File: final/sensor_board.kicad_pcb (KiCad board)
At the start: 2 copper layers, 75 parts, among them J1 USB_microB_2040002-1, J2 Arduino_ICSP, J3 Conn_01x02_Male, J6 BT CONFIG, SW1 SW_DIP_x01, U1 NC7SZ04P5X, U10 BQ24075, U11 BQ27441-G1, U2 MCP1702T-3302E/CBCT-ND, U3 TXS0104E, U4 TPS61200DRC, U5 FT232RL, U6 RN4871, U7 TPS2113ADRBR, U8 US5881, U9 ATMEGA328PB-ANR, Y1 16MHz

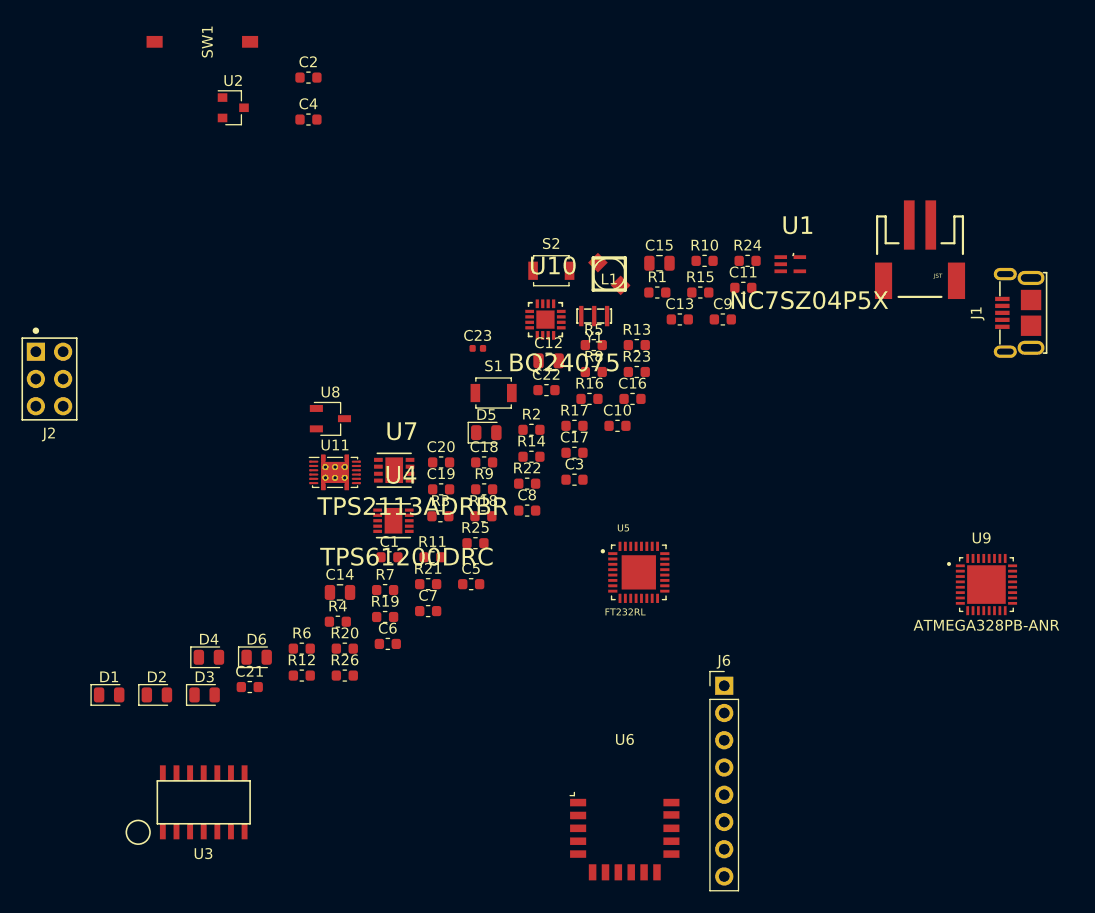
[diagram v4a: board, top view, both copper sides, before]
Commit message: sensor board layout complete
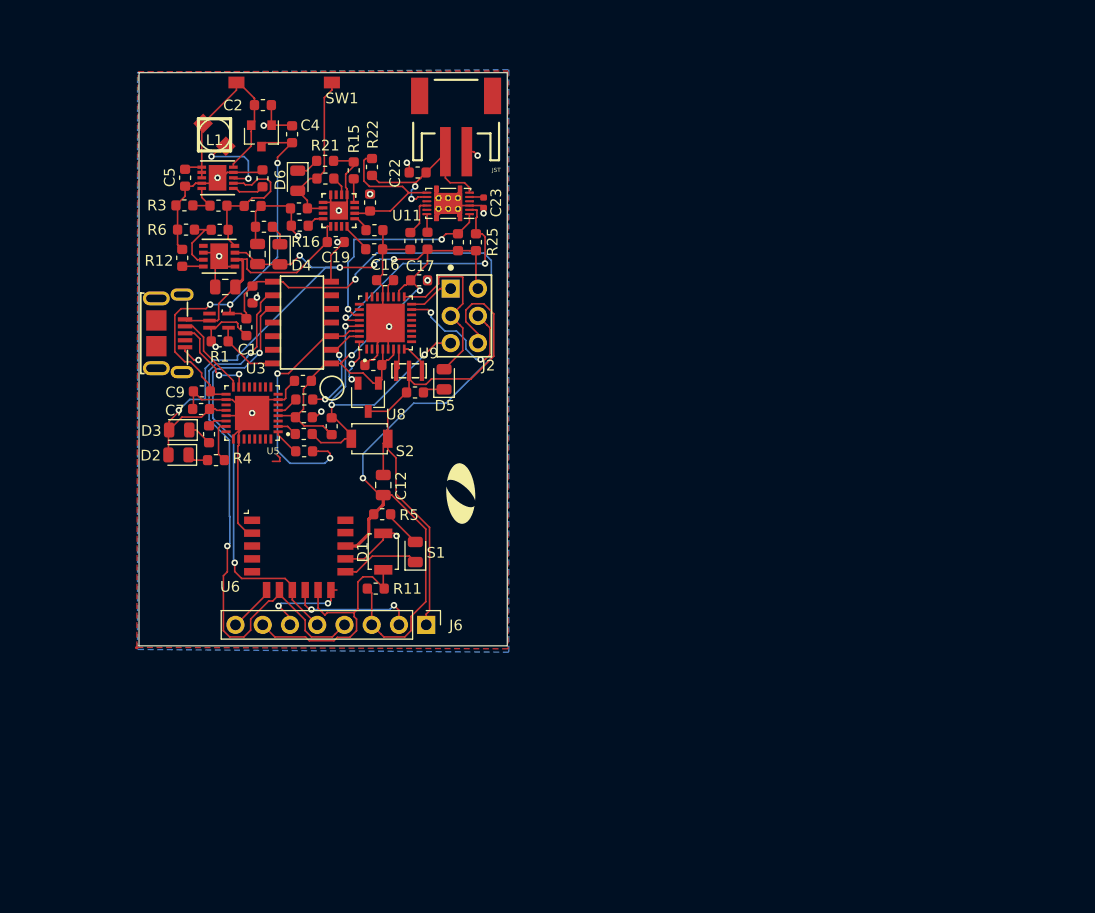
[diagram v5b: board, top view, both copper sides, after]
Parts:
- added OlinLogo: G***, mp3b:OlinLogo, F.Cu at (148.6, 100.7)
- moved J1 81.6 mm to (120.2, 85.8), turned to 270 degrees
- moved U9 61.1 mm to (141.6, 84.8), turned to 90 degrees
- moved U1 53.5 mm to (126.1, 84.6)
- moved C9 49.0 mm to (124.5, 91.2), turned to 180 degrees
- moved C21 46.5 mm to (140.2, 73.6), turned to 270 degrees
- moved C11 46.4 mm to (129.2, 73.9)
- moved C5 46.3 mm to (122.9, 71.2), turned to 270 degrees
- moved U3 45.7 mm to (133.8, 84.7), turned to 90 degrees
- moved J3 45.5 mm to (148.2, 65.1), turned to 0 degrees
- moved R10 45.3 mm to (126.1, 76.1)
- moved D6 44.6 mm to (133.4, 71.5), turned to 270 degrees
- moved R26 41.3 mm to (145.5, 77.1), turned to 270 degrees
- moved R1 41.0 mm to (126.1, 86.5), turned to 180 degrees
- moved R21 40.6 mm to (136.0, 69.7)
- moved R6 40.5 mm to (123.0, 76.1)
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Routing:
- net GND: track 0.00 -> 180.7 mm, vias 0 -> 18
- net +3V3: track 0.00 -> 127.4 mm, vias 0 -> 5
- net +5V: track 0.00 -> 101.4 mm, vias 0 -> 7
- net /RX: track 0.00 -> 54.4 mm, vias 0 -> 2
- net /TX: track 0.00 -> 40.2 mm, vias 0 -> 2
- net /RESET: track 0.00 -> 30.9 mm, vias 0 -> 3
- net /~RST: track 0.00 -> 24.8 mm
- net /D0: track 0.00 -> 24.2 mm, vias 0 -> 2
- net /UART_EN: track 0.00 -> 23.0 mm
- net /A5: track 0.00 -> 22.5 mm, vias 0 -> 2
- net Net-(C2-Pad1): track 0.00 -> 21.4 mm
- net /A4: track 0.00 -> 20.3 mm, vias 0 -> 2
- net /BATTERY: track 0.00 -> 17.4 mm, vias 0 -> 2
- net /D13: track 0.00 -> 16.9 mm
- net /VIN: track 0.00 -> 15.3 mm
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- added copper zone on F.Cu, net +3V3
- added copper zone on B.Cu, net GND
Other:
- board outline added: 34.3 x 53.4 mm
- net class Default: via_dia 0.8 -> 0.6096; via_drill 0.4 -> 0.3048

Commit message: sensor board final fix and is now ready for fab
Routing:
- net GND: track 180.7 -> 151.6 mm, vias 18 -> 23
- net +3V3: track 127.4 -> 139.0 mm
- net +5V: track 101.4 -> 108.6 mm
- net /D11: track 14.2 -> 7.99 mm, vias 2 -> 1
- net /CTS: track 8.87 -> 8.31 mm

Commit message: text added
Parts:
- moved OlinLogo 1.25 mm to (147.4, 100.9)
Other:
- board text added: "Ariana Olson, Kevin Guo, Leo Liu"
- board text added: "Olin College Eclectronics Final Project"
- board text added: "Sensor Board"
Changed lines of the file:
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@@
   (general
     (thickness 1.6)
-    (drawings 4)
+    (drawings 7)
     (tracks 840)
     (zones 0)
@@
   )
   (setup
-    (last_trace_width 0.254)
+    (last_trace_width 0.25)
     (user_trace_width 0.1524)
     (user_trace_width 0.254)
@@
   )
   (module mp3b:OlinLogo (layer F.Cu)
-    (at 148.61032 100.6856 90)
+    (at 147.38604 100.9396 90)
     (descr "Imported from OlinLogo.svg")
     (tags svg2mod)
@@
     )
   )
+  (gr_text "Ariana Olson, Kevin Guo, Leo Liu" (at 135.79348 65.62852) (layer B.SilkS)
+    (effects (font (size 1.5 1.27) (thickness 0.3) italic) (justify mirror))
+  )
+  (gr_text "Olin College Eclectronics Final Project" (at 150.6728 102.16388 90) (layer F.SilkS)
+    (effects (font (size 1.143 0.762) (thickness 0.1905)))
+  )
+  (gr_text "Sensor Board\n" (at 122.49912 106.48188 90) (layer F.SilkS)
+    (effects (font (size 1.5 1.5) (thickness 0.3)))
+  )
   (gr_line (start 118.618 114.8842) (end 118.618 61.44768) (layer Edge.Cuts) (width 0.1))
